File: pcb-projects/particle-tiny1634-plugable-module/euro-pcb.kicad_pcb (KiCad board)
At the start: 2 copper layers, 157.5 x 73.7 mm, 128 parts, among them IC1 ATTINY1634-SU, P1 INTERFACE, P2 MCU_TEST

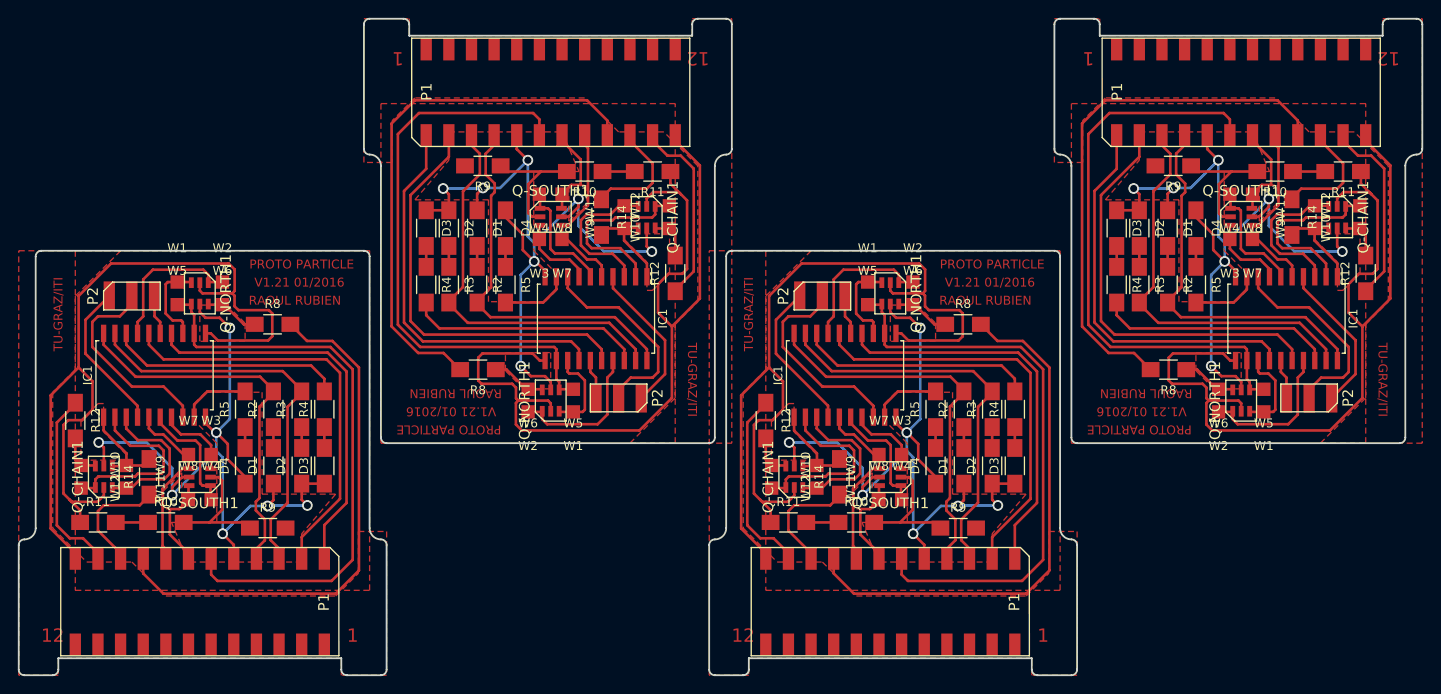
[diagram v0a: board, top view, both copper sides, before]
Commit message: updated euro pcb
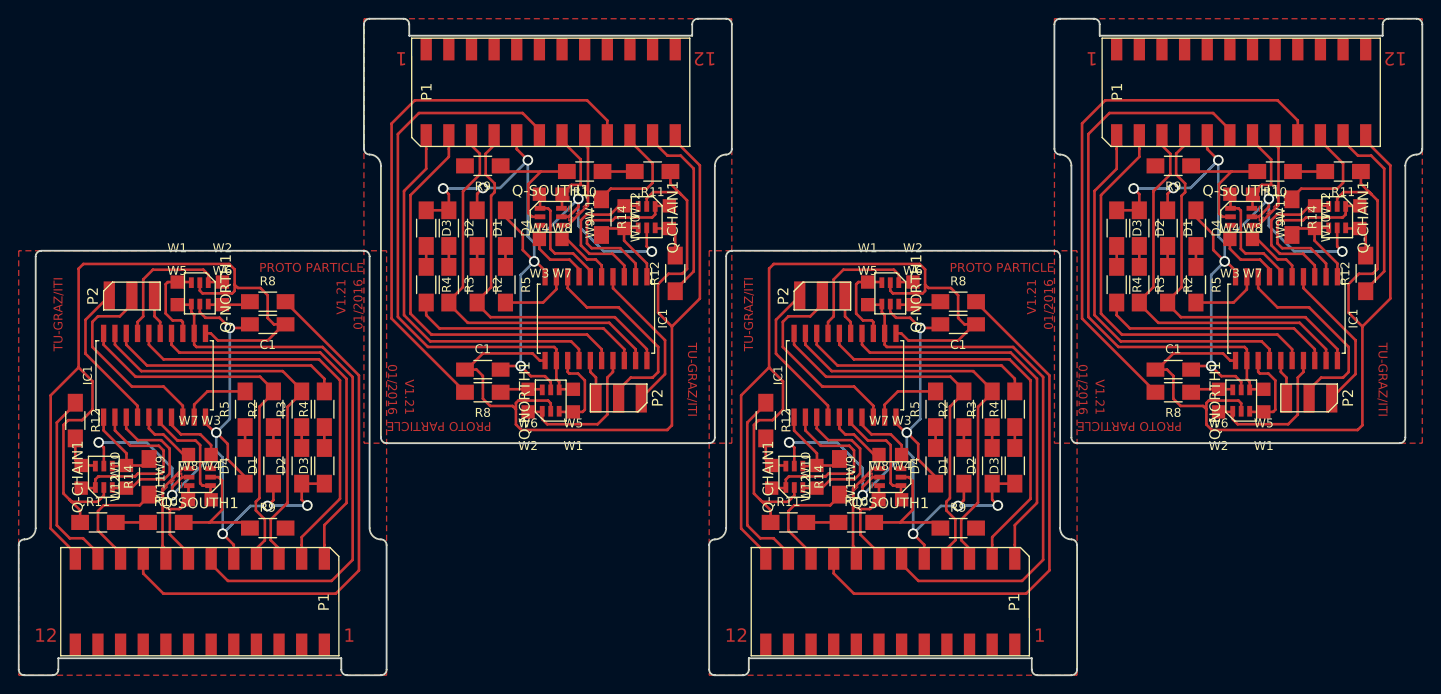
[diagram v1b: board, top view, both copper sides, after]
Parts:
- removed the R8 at (170.7, 101.0)
- removed the R8 at (193.8, 106.0)
- removed the R8 at (116.3, 106.0)
- added C1: 100nF, Capacitors_SMD:C_1206_HandSoldering, F.Cu at (170.2, 101.0)
- added C1: 100nF, Capacitors_SMD:C_1206_HandSoldering, F.Cu at (194.3, 106.0)
- added C1: 100nF, Capacitors_SMD:C_1206_HandSoldering, F.Cu at (116.8, 106.0)
- added C1: 100nF, Capacitors_SMD:C_1206_HandSoldering, F.Cu at (92.7, 101.0)
- added R8: 0R, Resistors_SMD:R_1206_HandSoldering, F.Cu at (170.2, 98.4)
- added R8: 0R, Resistors_SMD:R_1206_HandSoldering, F.Cu at (194.3, 108.6)
- added R8: 0R, Resistors_SMD:R_1206_HandSoldering, F.Cu at (116.8, 108.6)
- moved R8 2.60 mm to (92.7, 98.4)
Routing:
- net VCC: track 478.5 -> 495.0 mm
- net GND: track 344.8 -> 354.5 mm
- net /RX-NORTH: track 262.2 -> 257.4 mm
- net /SCK: track 186.6 -> 184.7 mm
- net /RESET: track 176.7 -> 174.8 mm
- removed copper zone on F.Cu, net (none)
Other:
- board text added: "01/2016"
- board text added: "V1.21"
- board text removed: "RAOUL RUBIEN"
- board text removed: "V1.21 01/2016"

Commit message: minor change: updated MCU power supply decoupling and euro pcb
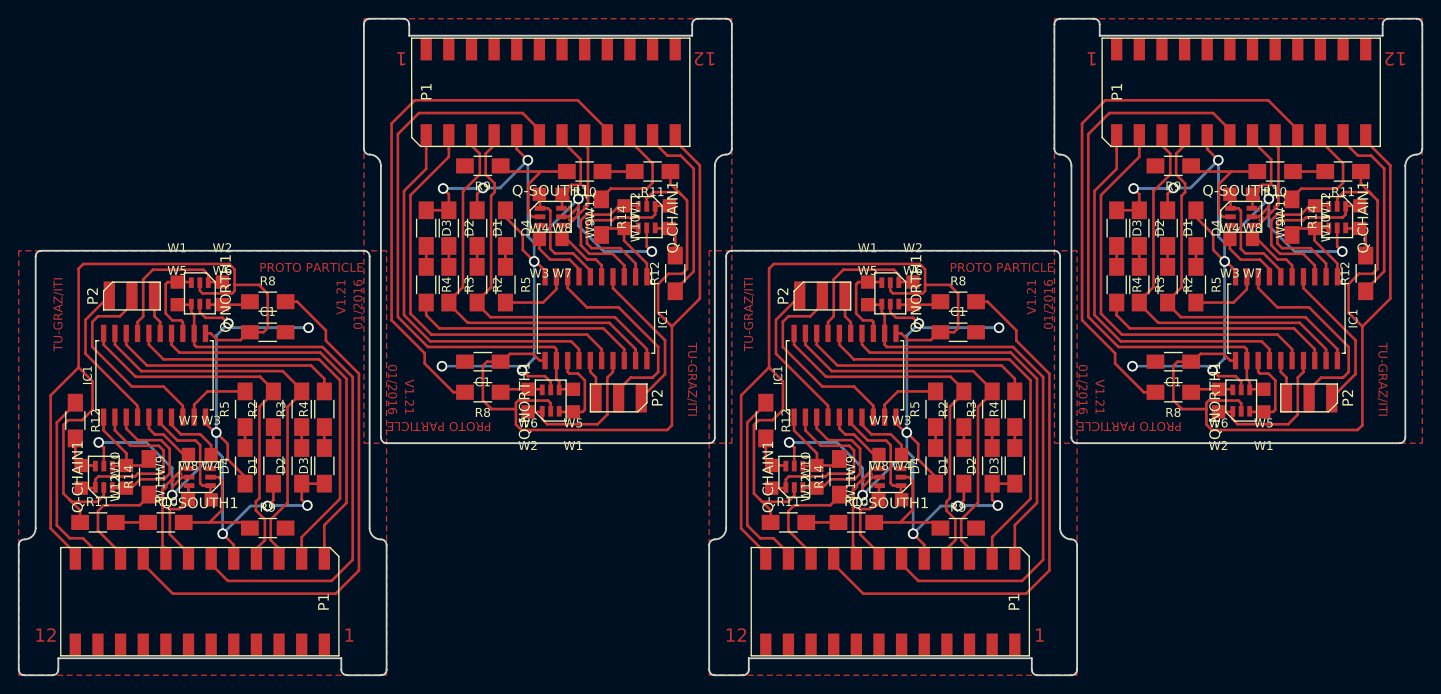
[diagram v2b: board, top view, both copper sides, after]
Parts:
- removed the C1 at (170.2, 101.0)
- removed the C1 at (194.3, 106.0)
- removed the C1 at (116.8, 106.0)
- added C1: 100nF, Capacitors_SMD:C_1206_HandSoldering, F.Cu at (170.2, 101.9)
- added C1: 100nF, Capacitors_SMD:C_1206_HandSoldering, F.Cu at (194.3, 105.2)
- added C1: 100nF, Capacitors_SMD:C_1206_HandSoldering, F.Cu at (116.8, 105.2)
- moved C1 0.89 mm to (92.7, 101.9), turned to 0 degrees
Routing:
- net GND: track 354.5 -> 381.8 mm, vias 28 -> 32
- net VCC: track 495.0 -> 481.9 mm
- net /TX-NORTH: track 265.9 -> 266.5 mm
